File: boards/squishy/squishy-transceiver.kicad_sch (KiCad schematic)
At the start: 99 parts, among them Q2 Q_PMOS_DGS, Q3 Q_DUAL_PMOS_S1G1D2S2G2D1, Q4 Q_DUAL_PMOS_S1G1D2S2G2D1, U1 THVD1452DGSR, U10 THVD1452DGSR, U11 FXL4TD245BQX, U13 THVD1452DGSR, U15 THVD1452DGSR, U16 FXL4TD245BQX, U17 THVD1452DGSR, U18 THVD1452DGSR, U2 FXL4TD245BQX, U20 FXL4TD245BQX, U21 THVD1452DGSR, U22 THVD1452DGSR, U23 FXL4TD245BQX, U24 THVD1452DGSR, U25 THVD1452DGSR, U27 FXL4TD245BQX, U28 THVD1452DGSR, U29 THVD1452DGSR, U30 FXL4TD245BQX, U31 THVD1452DGSR, U32 THVD1452DGSR, U33 FXL4TD245BQX, U34 THVD1452DGSR, U4 THVD1452DGSR, U6 THVD1452DGSR, U8 FXL4TD245BQX, U9 THVD1452DGSR

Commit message: hardware: cleanup and revamp for squishy rev2
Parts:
- removed Q2: Q_PMOS_DGS, Package_TO_SOT_SMD:SOT-323_SC-70, symbol Device:Q_PMOS_GSD
- removed Q3, Q4: Q_DUAL_PMOS_S1G1D2S2G2D1, Package_TO_SOT_SMD:SOT-363_SC-70-6, symbol Device:Q_DUAL_PMOS_S1G1D2S2G2D1
- removed R11, R12, R15, R18, R21, R22, R23, R24, R25, R26, R27, R28, R3, R4, R5, R6, R8, R9: 150, Resistor_SMD:R_0603_1608Metric, symbol Device:R_Small
- removed R29, R30, R32, R35, R37, R38, R40, R44, R46, R65, R67, R68, R70, R73, R75: 10k, Resistor_SMD:R_0603_1608Metric, symbol Device:R_Small
- removed R31, R33, R34, R36, R39, R41, R42, R43, R45, R47, R48, R49, R50, R51, R54, R55, R56, R58, R59, R60, R61, R63, R64, R66, R69, R71, R74, R76, R78, R79, R80, R81, R82, R83, R84, R85: 330, Resistor_SMD:R_0603_1608Metric, symbol Device:R_Small
- removed U1, U10, U13, U15, U17, U18, U21, U22, U24, U25, U28, U29, U31, U32, U34, U4, U6, U9: THVD1452DGSR, Package_SO:VSSOP-10_3x3mm_P0.5mm, symbol lethalbit:THVD1452DGSR
- removed U11, U16, U2, U20, U23, U27, U30, U33, U8: FXL4TD245BQX, DX-MON:DQFN16_1EP_2.5x3.5mm_P0.5mm, symbol lethalbit:FXL4TD245BQX
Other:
- note removed: "+"
- note removed: "-"
- note removed: "RX"
- note removed: "SCSI Frontend Transciver"
- note removed: "SCSI Single-Ended Level Shifters"
- note removed: "TX"
- note removed: "Transmit Enable"
- title: (none) -> Squishy

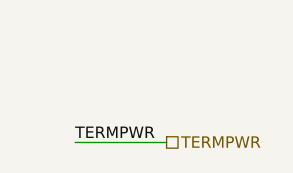
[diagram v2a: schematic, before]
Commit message: hardware: in the process of swapping out the hard-mount scsi connector for a mezzanine connector to allow for swapping out of connectors
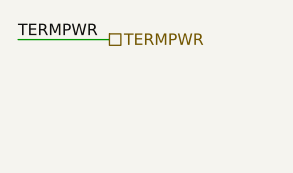
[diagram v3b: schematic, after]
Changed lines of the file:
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@@
     (company "Aki")
   )
-  (wire (pts (xy 33.02 30.48) (xy 22.86 30.48))
+  (wire (pts (xy 26.67 19.05) (xy 16.51 19.05))
     (stroke (width 0) (type default) (color 0 0 0 0))
   )
-  (label "TERMPWR" (at 22.86 30.48 0)
+  (label "TERMPWR" (at 16.51 19.05 0)
     (effects (font (size 1.27 1.27)) (justify left bottom))
   )
-  (hierarchical_label "TERMPWR" (shape passive) (at 33.02 30.48 0)
+  (hierarchical_label "TERMPWR" (shape passive) (at 26.67 19.05 0)
     (effects (font (size 1.27 1.27)) (justify left))
   )
